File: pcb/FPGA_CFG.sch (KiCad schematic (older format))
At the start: 5 parts, among them U4 iCE40-HX8K-CT256, U6 SERIAL_FLASH

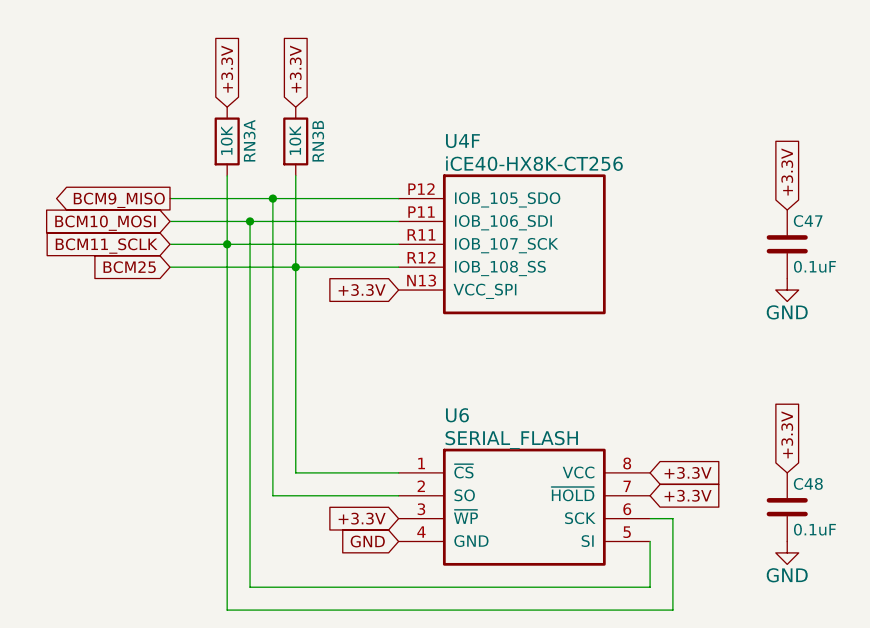
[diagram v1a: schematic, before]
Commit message: Most components placed. FPGA + SDRAM + routing placed off-board.
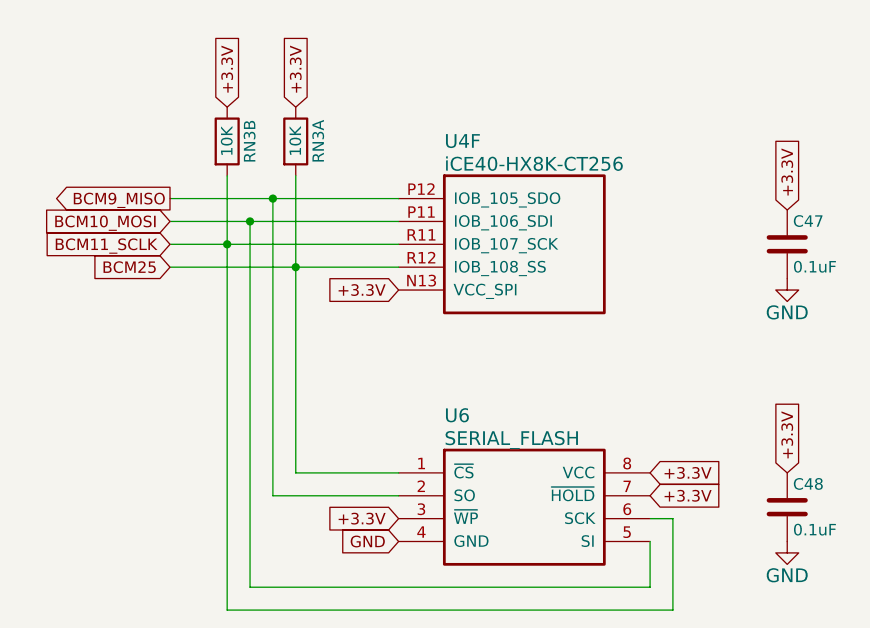
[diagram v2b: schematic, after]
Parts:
- C47, C48: footprint Capacitors_SMD:C_0603_HandSoldering -> Capacitors_SMD:C_0603
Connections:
- net BCM11_SCLK: now also RN3.2; no longer RN3.1
- net BCM25: now also RN3.1; no longer RN3.2
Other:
- moved on the sheet: RN3A, RN3B
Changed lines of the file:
@@
 F 0 "C47" H 7325 3800 50  0000 L CNN
 F 1 "0.1uF" H 7325 3600 50  0000 L CNN
-F 2 "Capacitors_SMD:C_0603_HandSoldering" H 7338 3550 30  0001 C CNN
+F 2 "Capacitors_SMD:C_0603" H 7338 3550 30  0001 C CNN
 F 3 "" H 7300 3700 60  0000 C CNN
 F 4 "08055C104KAT2A" H 7300 3700 60  0001 C CNN "manf#"
@@
 F 0 "C48" H 7325 4950 50  0000 L CNN
 F 1 "0.1uF" H 7325 4750 50  0000 L CNN
-F 2 "Capacitors_SMD:C_0603_HandSoldering" H 7338 4700 30  0001 C CNN
+F 2 "Capacitors_SMD:C_0603" H 7338 4700 30  0001 C CNN
 F 3 "" H 7300 4850 60  0000 C CNN
 F 4 "08055C104KAT2A" H 7300 4850 60  0001 C CNN "manf#"
@@
 L RN2 RN3
 U 1 1 55F0D803
-P 4850 3400
-F 0 "RN3" H 5000 3300 50  0000 C CNN
-F 1 "10K" H 5000 3400 50  0000 C CNN
-F 2 "XESS:CTS_742C043" H 4850 3400 50  0001 C CNN
-F 3 "" H 4850 3400 50  0000 C CNN
-	1    4850 3400
-	0    -1   -1   0
-$EndComp
-$Comp
-L RN2 RN3
-U 2 1 55F0D8A0
 P 5150 3400
 F 0 "RN3" H 5300 3300 50  0000 C CNN
@@
 F 2 "XESS:CTS_742C043" H 5150 3400 50  0001 C CNN
 F 3 "" H 5150 3400 50  0000 C CNN
-	2    5150 3400
+	1    5150 3400
+	0    -1   -1   0
+$EndComp
+$Comp
+L RN2 RN3
+U 2 1 55F0D8A0
+P 4850 3400
+F 0 "RN3" H 5000 3300 50  0000 C CNN
+F 1 "10K" H 5000 3400 50  0000 C CNN
+F 2 "XESS:CTS_742C043" H 4850 3400 50  0001 C CNN
+F 3 "" H 4850 3400 50  0000 C CNN
+	2    4850 3400
 	0    -1   -1   0
 $EndComp
@@
 1E 25 49 2A DA F6 C4 5C B7 0C C3 B9 A4 0A 98 09 FC 0D B0 92 CD 57 CD 1F 06 4E 04 26 A7 75 27 49
 52 39 26 13 73 DE C3 6C BE 70 B5 12 F8 16 86 73 8D C3 FF 03 63 F8 EE 2E BE 9A 04 B1 00 00 00 00
-49 45 4E 44 AE 42 60 82 D3
+49 45 4E 44 AE 42 60 82 E5
 EndData
 $EndBitmap

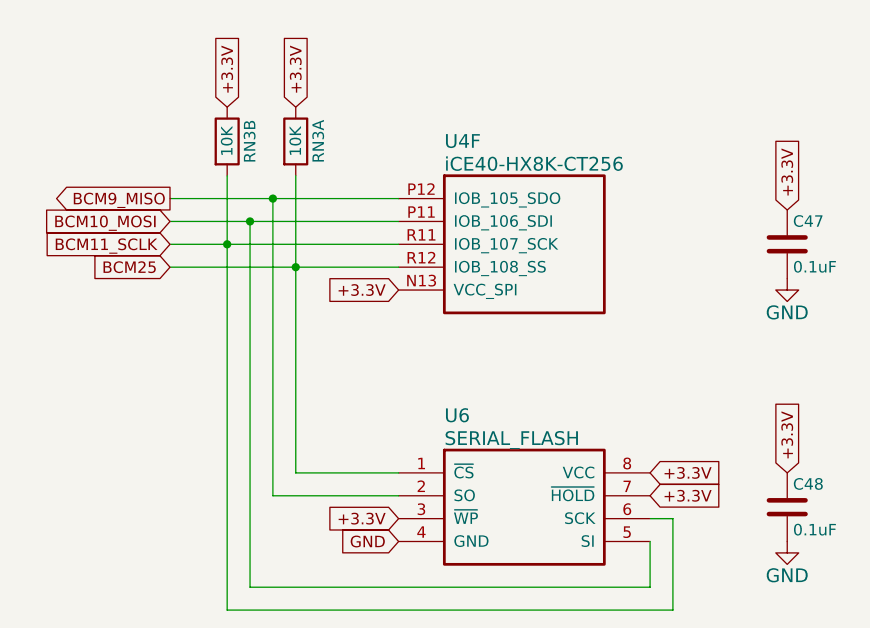
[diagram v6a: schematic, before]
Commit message: Spreading wires, arranging components.
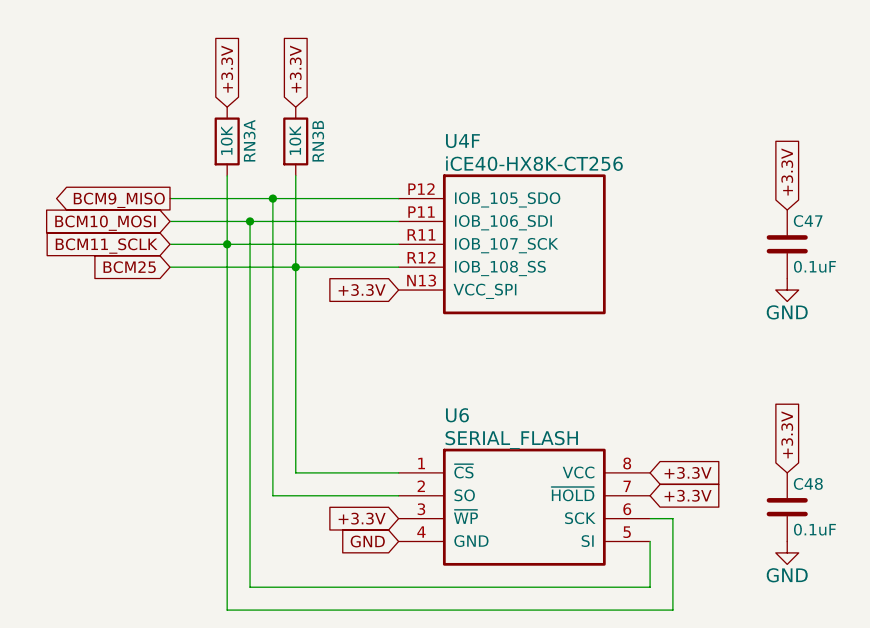
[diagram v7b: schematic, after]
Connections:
- net BCM11_SCLK: now also RN3.1; no longer RN3.2
- net BCM25: now also RN3.2; no longer RN3.1
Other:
- moved on the sheet: RN3A, RN3B
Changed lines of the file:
@@
 L RN2 RN3
 U 1 1 55F0D803
-P 5150 3400
-F 0 "RN3" H 5300 3300 50  0000 C CNN
-F 1 "10K" H 5300 3400 50  0000 C CNN
-F 2 "XESS:CTS_742C043" H 5150 3400 50  0001 C CNN
-F 3 "" H 5150 3400 50  0000 C CNN
-	1    5150 3400
-	0    -1   -1   0
-$EndComp
-$Comp
-L RN2 RN3
-U 2 1 55F0D8A0
 P 4850 3400
 F 0 "RN3" H 5000 3300 50  0000 C CNN
@@
 F 2 "XESS:CTS_742C043" H 4850 3400 50  0001 C CNN
 F 3 "" H 4850 3400 50  0000 C CNN
-	2    4850 3400
+	1    4850 3400
+	0    -1   -1   0
+$EndComp
+$Comp
+L RN2 RN3
+U 2 1 55F0D8A0
+P 5150 3400
+F 0 "RN3" H 5300 3300 50  0000 C CNN
+F 1 "10K" H 5300 3400 50  0000 C CNN
+F 2 "XESS:CTS_742C043" H 5150 3400 50  0001 C CNN
+F 3 "" H 5150 3400 50  0000 C CNN
+	2    5150 3400
 	0    -1   -1   0
 $EndComp
@@
 1E 25 49 2A DA F6 C4 5C B7 0C C3 B9 A4 0A 98 09 FC 0D B0 92 CD 57 CD 1F 06 4E 04 26 A7 75 27 49
 52 39 26 13 73 DE C3 6C BE 70 B5 12 F8 16 86 73 8D C3 FF 03 63 F8 EE 2E BE 9A 04 B1 00 00 00 00
-49 45 4E 44 AE 42 60 82 E6
+49 45 4E 44 AE 42 60 82 71
 EndData
 $EndBitmap
